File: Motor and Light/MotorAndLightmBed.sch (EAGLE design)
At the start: 97 parts, among them Q1 BSS84, Q3 BC846ASMD, Q4 220mA/50V/3.5Ω, Q5 220mA/50V/3.5Ω, Q6 220mA/50V/3.5Ω, Q7 220mA/50V/3.5Ω, U1 9DoF IMU, U2 LPC1768FBD100, X1 2510-, X2 2510-, X3 C-GRID-05-15-91, X4 C-GRID-05-15-91, X5 C-GRID-02-70553, X6 MINI-USB_4P-32005-101, Y1 32.768kHz

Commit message: Ethernet Chip added
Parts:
- added C15, C16: 100nF, rcl:C-USC0603
- added C17, C18: 100nF, resistor:C-USC0603
- added R14, R16, R17, R18: 49.9, rcl:R-US_R0603
- added U$2: DP83848JSQ/NOPB, DigiKey:DP83848JSQ/NOPB
- added X7: 22-23-2041, con-molex:22-23-2041
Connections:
- new net N$11: C18.1, U$2.AVDD33
- new net N$12: U$2.PFBOUT
- new net PFBOUT: C17.1, U$2.PFBIN1
- new net RD+: R16.1, U$2.RD+, X7-3.S
- new net RD-: R14.2, U$2.RD-, X7-4.S
- new net TD+: R18.1, U$2.TD+, X7-1.S
- new net TD-: R17.2, U$2.TD-, X7-2.S
- net +3V3: now also C15.1, C16.1, R14.1, R16.2, R17.1, R18.2
- net GND: now also C15.2, C16.2, C17.2, C18.2, U$2.AGND, U$2.AGND_2
- net SCL: now also U2.P0[20]/DTR1/SCL1
- net SDA: now also U2.P0[19]/DSR1/SDA1
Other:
- note added: "Add Ethernet"
- note added: "Analog"
- note added: "Digital into the Chip"
- moved on the sheet: J1, X1-1, X1-10, X1-2, X1-3, X1-4, X1-5, X1-6, X1-7, X1-8, X1-9, X2-1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

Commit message: First Version Completed
Several Questions remain, mbed microcontroller not included, TD, RD, +-
and D+- from ethernet Phy and main chip not connected, some pin
connection requires verification.
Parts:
- removed X6: MINI-USB_4P-32005-101, con-cypressindustries:MINI-USB_4P-32005-101
- added C19, C20, C23, C24, C25, C26: 100nF, resistor:C-USC0603
- added C21, C22: 10uF, SparkFun-Capacitors:10UF-POLAR-0603-6.3V-20%(TANT)
- added C27: 100nF, rcl:C-USC0603
- added D1, D2, D3, D4: BLUE, SparkFun-LED:LED-BLUE0603
- added J6: 6_PIN_SERIAL_CABLEPTH, SparkFun-Connectors:6_PIN_SERIAL_CABLEPTH
- added R19: 4870, rcl:R-US_R0603
- added R20: 2.2k, rcl:R-US_R0603
- added R21, R22, R23, R24: 220, resistor:R-US_R0603
- added R25, R26, R27, R28: 10k, SparkFun-Resistors:10KOHM-0603-1/10W-1%
- added R29: 100k, SparkFun-Resistors:100KOHM-0603-1/10W-1%
- added Y2: OSCILLATORSMD-5X3-50MHz, SparkFun-Clocks:OSCILLATORSMD-5X3
- added Y3: OSCILLATORSMD-5X3-12MHz, SparkFun-Clocks:OSCILLATORSMD-5X3
- U$1: value (none) -> 10uH
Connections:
- net SCON renamed TGT_SCON
- removed net N$12: U$2.PFBOUT
- removed net N$56: T1.C
- removed net N$57: T9.C
- removed net N$58: T7.C
- removed net RESET: C12.1, R15.1, S1.1
- removed net RXD: J5.7, U2.P0[25]/AD0[2]/I2SRX_SDA/TXD3
- removed net TCK: J5.4, U2.TCK/SWDCLK
- new net CLK: U$2.X1, U2.P1[15]/ENET_REF_CLK, Y2.OUT
- new net ETH_OSC_EN: U2.P1[27]/CLKOUT/!USB_OVRCR/CAP0[1], Y2.EN
- new net ETH_RST: U$2.RESET_N, U2.P1[28]/MCOA2/PCAP1[0]/MAT0[0]
- new net LED-1: R21.1, U2.P1[18]/USB_UP_LED/PWM1[1]/CAP1[0]
- new net LED-2: R22.1, U2.P1[20]/MCI0/PWM1[2]/SCK0
- new net LED-3: R23.1, U2.P1[21]/!MCABORT/PWM1[3]/SSEL0
- new net LED-4: R24.1, U2.P1[23]/MCI1/PWM1[4]/MISO0
- new net LED_LINK: U$2.LED_LINK/AN0, U2.P1[25]/MCOA1/MAT1[1]
- new net LED_SPEED: U$2.LED_SPEED/AN1, U2.P1[26]/MCOB1/PWM1[6]/CAP0[0]
- new net N$14: R19.1, U$2.RBIAS
- new net N$16: R20.2, U$2.RX_DV/MII_MODE
- new net N$17: D1.A, R21.2
- new net N$18: D2.A, R22.2
- new net N$19: D3.A, R23.2
- new net N$20: D4.A, R24.2
- new net RTCK: J5.7, R25.1, U2.RTCK
- new net TCLK: J5.4, R26.1, U2.TCK/SWDCLK
- new net TGT_P1.0: U$2.TXD_0, U2.P1[0]/ENET_TXD0
- new net TGT_P1.1: U$2.TXD_1, U2.P1[1]/ENET_TXD1
- new net TGT_P1.10: U$2.RXD_1/PHYAD2, U2.P1[10]/ENET_RXD1
- new net TGT_P1.14: U$2.RX_ER/MDIX_EN, U2.P1[14]/ENET_RX_ER
- new net TGT_P1.16: U$2.MDC, U2.P1[16]/ENET_MDC
- new net TGT_P1.17: U$2.MDIO, U2.P1[17]/ENET_MDIO
- new net TGT_P1.4: U$2.TX_EN, U2.P1[4]/ENET_TX_EN
- new net TGT_P1.8: U$2.CRS/CRS_DV/LED_CFG, U2.P1[8]/ENET_CRS
- new net TGT_P1.9: U$2.RXD_0/PHYAD1, U2.P1[9]/ENET_RXD0
- new net TGT_RXD: J6.3, U2.P0[3]/RXD0/AD0[6]
- new net TGT_TXD: J6.2, U2.P0[2]/TXD0/AD0[7]
- new net TRST: U2.!TRST
- net +3V3: now also C20.1, C22.+, C23.1, C24.1, C26.1, R20.1, R25.2, R27.2, R28.1, R29.2, U$2.IOVDD33, U$2.IOVDD33_2, Y2.VCC, Y3.EN, Y3.VCC; no longer J5.1
- net 12MHZ: now also Y3.OUT
- net 1S1: now also U2.P0[15]/TXD1/SCK0/SCK
- net 1S2: now also U2.P0[16]/RXD1/SSEL0/SSEL
- net 1S3: now also U2.P0[17]/CTS1/MISO0/MISO
- net 2S1: now also U2.P0[18]/DCD1/MOSI0/MOSI
- net 2S2: now also U2.P0[21]/RI1/RD1
- net 2S3: now also U2.P0[22]/RTS1/TD1
- net BATTIN: now also U2.P2[6]/PCAP1[0]/RI1/TRACECLK
- net GND: now also C19.2, C20.2, C21.-, C22.-, C23.2, C24.2, C25.2, C26.2, C27.2, D1.C, D2.C, D3.C, D4.C, J6.6, R19.2, R26.2, T1.C, T7.C, T9.C, U$2.DAP, U$2.DGND, U$2.IOGND, U1.AD0/SDO, Y2.GND, Y3.GND
- net LDIR: now also U2.P2[1]/PWM1[2]/RXD1
- net LDISABLE: now also U2.P2[2]/PWM1[3]/CTS1/TRACEDATA[3]
- net LEA3: now also U2.P0[4]/I2SRX_CLK/RD2/CAP2[0]
- net LEB3: now also U2.P0[5]/I2SRX_WS/TD2/CAP2[1]
- net LSPEED: now also U2.P2[0]/PWM1[1]/TXD1
- net NRESET: now also C12.1, C27.1, R15.1, R29.1, S1.1, U2.!RESET; no longer U2.!TRST
- net PFBOUT: now also C19.1, C21.+, C25.1, U$2.PFBIN2, U$2.PFBOUT
- net RDIR: now also U2.P2[4]/PWM1[5]/DSR1/TRACEDATA[1]
- net RDISABLE: now also U2.P2[5]/PWM1[6]/DTR1/TRACEDATA[0]
- net REA3: now also U2.P0[6]/I2SRX_SDA/SSEL1/MAT2[0]
- net REB3: now also U2.P0[7]/I2STX_CLK/SCK1/MAT2[1]
- net RSPEED: now also U2.P2[3]/PWM1[4]/DCD1/TRACEDATA[2]
- net TDI: now also R28.2
- net TMS: now also R27.1
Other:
- note added: "D+ and D- going in/out any stuff?"
- note added: "Questionable"
- note added: "need to verify this"
- note removed: "Add Ethernet"
- note removed: "Analog"
- note removed: "Digital into the Chip"
- moved on the sheet: C15, C16, R14, R16, R17, R18, X3-1, X3-2, X3-3, X3-4, X3-5, X4-1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

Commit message: final version v2.0
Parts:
- removed X7: 22-23-2041, con-molex:22-23-2041
- added C28, C29: 0.1uF, SparkFun-Capacitors:0.1UF-0603-25V-(+80/-20%)
- added J7: (no value), SparkFun-Connectors:USB_MICRO-B_FEMALE-SMT
- added R30, R31: 33, SparkFun-Resistors:33OHM-0603-1/10W-1%
- added R32, R33: 150, SparkFun-Resistors:150OHM-0603-1/10W-1%
- added U$3: V_REG_LD1117VXX, SparkFun-IC-Power:V_REG_LD1117VXX
- added X6: SI-50170, con-stewart:SI-50170
- R19: value 4870 -> 4.87k
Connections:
- net CLK renamed 50MHZ
- new net ETH_LED1: R32.2, X6.A
- new net ETH_LED2: R33.2, X6.A1
- new net N$15: R33.1, U2.P0[5]/I2SRX_WS/TD2/CAP2[1]
- net +3V3: now also C18.1, C28.1, C29.1, U$2.AVDD33, U$3.OUT, X6.RCT, X6.TCT
- net +5V: now also J7.VBUS, U$3.IN
- net BATTIN: now also U2.P0[26]/AD0[3]/AOUT/RXD3; no longer U2.P2[6]/PCAP1[0]/RI1/TRACECLK
- net GND: now also C28.2, C29.2, J7.GND, J7.SHIELD, U$3.GND, X6.C, X6.C1, X6.S1, X6.S2
- net GYRO_INT: now also U2.P2[10]/!EINT0/NMI
- net LEA3: now also U2.P0[8]/I2STX_WS/MISO1/MAT2[2]; no longer U2.P0[4]/I2SRX_CLK/RD2/CAP2[0]
- net LEB3: now also U2.P0[9]/I2STX_SDA/MOSI1/MAT2[3]; no longer U2.P0[5]/I2SRX_WS/TD2/CAP2[1]
- net LPC_D+: now also J7.D+, R30.1, R30.2
- net LPC_D-: now also J7.D-, R31.1, R31.2
- net N$11: now also R32.1, U2.P0[4]/I2SRX_CLK/RD2/CAP2[0]; no longer C18.1, U$2.AVDD33
- net RD+: now also X6.RD+; no longer X7-3.S
- net RD-: now also X6.RD-; no longer X7-4.S
- net TD+: now also X6.TD+; no longer X7-1.S
- net TD-: now also X6.TD-; no longer X7-2.S
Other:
- note removed: "D+ and D- going in/out any stuff?"
- note removed: "Questionable"
- moved on the sheet: C19, C21, R19

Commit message: Motor and Light Initial Submit
Primary structure completed, resistors and capacitors remained to add
and some general arrangement issues to be resolved.
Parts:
- removed OK2: MOCD208M, optocoupler:MOCD208M
- removed R12, R13, R3, R6: 1k, SparkFun-Resistors:1KOHM-0603-1/10W-1%
- removed R20: 2.2k, rcl:R-US_R0603
- added R34: 200, SparkFun-Resistors:200OHM-0603-1/10W-1%
- C15, C16: value 100nF -> 0.1uF; device rcl:C-USC0603 -> SparkFun-Capacitors:0.1UF-0603-25V-5%
- C17, C18, C19, C20, C24, C25, C26: value 100nF -> 0.1uF; device resistor:C-USC0603 -> SparkFun-Capacitors:0.1UF-0603-25V-5%
- C23: value 100nF -> 0.1uF; device resistor:C-USC0603 -> SparkFun-Capacitors:0.1UF-0603-25V-(+80/-20%)
- C27: value 100nF -> 0.1uF; device rcl:C-USC0603 -> SparkFun-Capacitors:0.1UF-0603-25V-(+80/-20%)
- R21, R22, R23: value 220 -> 200; device resistor:R-US_R0603 -> SparkFun-Resistors:200OHM-0603-1/10W-1%
- R24: value 220 -> 2.2k; device resistor:R-US_R0603 -> SparkFun-Resistors:2.2KOHM-0603-1/10W-1%
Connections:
- removed net LDISABLEI: R6.1
- removed net N$5: OK2A.A, R3.2
- removed net N$8: OK2B.A, R6.2
- removed net RDISABLEI: R3.1
- removed net VDD: C5.1, C6.1, C7.1, C8.1, C9.+, U$1.P$2, U2.NC, U2.VBAT, U2.VDD, U2.VDD_2, U2.VDD_3, U2.VDD_4, U2.VDD_5, U2.VDD_6
- net +3V3: now also C15.2, C16.2, C20.2, C23.2, C5.1, C6.1, C7.1, C8.1, C9.+, R24.2, U$1.P$2, U2.NC, U2.VBAT, U2.VDD, U2.VDD_2, U2.VDD_3, U2.VDD_4, U2.VDD_5, U2.VDD_6; no longer C15.1, C16.1, C20.1, C23.1, R20.1
- net GND: now also C15.1, C16.1, C17.1, C20.1, C23.1; no longer C15.2, C16.2, C17.2, C20.2, C23.2, OK2A.C, OK2B.C
- net LDISABLE: no longer OK2B.EMIT, R12.2
- net LED-1: now also R34.1; no longer R21.1
- net LED-2: now also R21.1; no longer R22.1
- net LED-3: now also R22.1; no longer R23.1
- net LED-4: now also R23.1; no longer R24.1
- net LGND: no longer R12.1
- net LVCC: no longer OK2B.COL
- net N$16: now also R24.1; no longer R20.2
- net N$17: now also R34.2; no longer R21.2
- net N$18: now also R21.2; no longer R22.2
- net N$19: now also R22.2; no longer R23.2
- net N$20: now also R23.2; no longer R24.2
- net PFBOUT: now also C17.2; no longer C17.1
- net RDISABLE: no longer OK2A.EMIT, R13.2
- net RGND: no longer R13.1
- net RVCC: no longer OK2A.COL
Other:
- moved on the sheet: C15, C16, C17, C20, C23, R21, R22, R23, R24

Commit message: Updated Board Design
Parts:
- removed U$3: V_REG_LD1117VXX, SparkFun-IC-Power:V_REG_LD1117VXX
- added CR1: LD1117S33TR, LD1117:LD1117S33TR
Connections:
- new net USB_D+: C10.1, R1.2, R30.2, U2.P0[29]/USB_D+
- new net USB_D-: C11.1, R31.2, U2.P0[30]/USB_D?
- net +3V3: now also CR1.OUTPUT; no longer U$3.OUT
- net +5V: now also CR1.INPUT; no longer U$3.IN
- net GND: now also CR1.GROUND; no longer U$3.GND
- net LEA3: now also U2.P2[11]/!EINT1/I2STX_CLK; no longer U2.P0[8]/I2STX_WS/MISO1/MAT2[2]
- net LPC_D+: no longer C10.1, R1.2, R30.2, U2.P0[29]/USB_D+
- net LPC_D-: no longer C11.1, R31.2, U2.P0[30]/USB_D?
- net REA3: now also U2.P2[12]/!EINT2/I2STX_WS; no longer U2.P0[6]/I2SRX_SDA/SSEL1/MAT2[0]
- net REB3: now also U2.P0[8]/I2STX_WS/MISO1/MAT2[2]; no longer U2.P0[7]/I2STX_CLK/SCK1/MAT2[1]

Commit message: update
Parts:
- added R3, R6: 2700, SparkFun-Resistors:3.9KOHM-0603-1/10W-1%
- added T10: (no value), transistor:-NPN-TO220V
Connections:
- new net N$24: J4.1, R6.1, T10.C
- net +12V: now also R6.2
- net ESTOP: now also R3.2, U2.P0[0]/RD1/TXD3/SDA1
- net GND: now also R3.1, T10.E
- net SLIGHT: now also T10.B, U2.P0[1]/TD1/RXD3/SCL1; no longer J4.1
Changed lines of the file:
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@@
 <part name="C23" library="SparkFun-Capacitors" deviceset="0.1UF" device="-0603-25V-(+80/-20%)" value="0.1uF"/>
 <part name="CR1" library="LD1117" deviceset="LD1117S33TR" device=""/>
+<part name="R3" library="SparkFun-Resistors" deviceset="3.9KOHM" device="-0603-1/10W-1%" value="2700"/>
+<part name="GND6" library="supply1" deviceset="GND" device=""/>
+<part name="T10" library="transistor" deviceset="*-NPN-" device="TO220V"/>
+<part name="GND9" library="supply1" deviceset="GND" device=""/>
+<part name="R6" library="SparkFun-Resistors" deviceset="3.9KOHM" device="-0603-1/10W-1%" value="2700"/>
+<part name="P+3" library="supply1" deviceset="+12V" device=""/>
 </parts>
 <sheets>
@@
 <instance part="C23" gate="G$1" x="276.86" y="101.6"/>
 <instance part="CR1" gate="A" x="114.3" y="177.8"/>
+<instance part="R3" gate="G$1" x="505.46" y="355.6" rot="R90"/>
+<instance part="GND6" gate="1" x="505.46" y="345.44"/>
+<instance part="T10" gate="G$1" x="444.5" y="358.14"/>
+<instance part="GND9" gate="1" x="447.04" y="342.9"/>
+<instance part="R6" gate="G$1" x="447.04" y="373.38" rot="R90"/>
+<instance part="P+3" gate="1" x="447.04" y="386.08"/>
 </instances>
 <busses>
@@
 <wire x1="177.8" y1="175.26" x2="180.34" y2="175.26" width="0.1524" layer="91"/>
 </segment>
+<segment>
+<pinref part="R3" gate="G$1" pin="1"/>
+<pinref part="GND6" gate="1" pin="GND"/>
+<wire x1="505.46" y1="350.52" x2="505.46" y2="347.98" width="0.1524" layer="91"/>
+</segment>
+<segment>
+<pinref part="T10" gate="G$1" pin="E"/>
+<pinref part="GND9" gate="1" pin="GND"/>
+<wire x1="447.04" y1="353.06" x2="447.04" y2="345.44" width="0.1524" layer="91"/>
+</segment>
 </net>
 <net name="N$1" class="0">
@@
 <wire x1="462.28" y1="332.74" x2="469.9" y2="332.74" width="0.1524" layer="91"/>
 </segment>
+<segment>
+<pinref part="P+3" gate="1" pin="+12V"/>
+<pinref part="R6" gate="G$1" pin="2"/>
+<wire x1="447.04" y1="383.54" x2="447.04" y2="378.46" width="0.1524" layer="91"/>
+</segment>
 </net>
 <net name="RED" class="0">
@@
 <segment>
 <pinref part="X5" gate="-1" pin="S"/>
-<wire x1="510.54" y1="365.76" x2="500.38" y2="365.76" width="0.1524" layer="91"/>
+<wire x1="510.54" y1="365.76" x2="505.46" y2="365.76" width="0.1524" layer="91"/>
 <label x="500.38" y="365.76" size="1.778" layer="95"/>
+<pinref part="R3" gate="G$1" pin="2"/>
+<wire x1="505.46" y1="365.76" x2="500.38" y2="365.76" width="0.1524" layer="91"/>
+<wire x1="505.46" y1="365.76" x2="505.46" y2="360.68" width="0.1524" layer="91"/>
+</segment>
+<segment>
+<pinref part="U2" gate="A" pin="P0[0]/RD1/TXD3/SDA1"/>
+<wire x1="121.92" y1="231.14" x2="106.68" y2="231.14" width="0.1524" layer="91"/>
+<label x="106.68" y="231.14" size="1.778" layer="95"/>
 </segment>
 </net>
 <net name="SLIGHT" class="0">
 <segment>
-<pinref part="J4" gate="G$1" pin="1"/>
-<wire x1="469.9" y1="365.76" x2="462.28" y2="365.76" width="0.1524" layer="91"/>
-<label x="459.74" y="365.76" size="1.778" layer="95"/>
+<pinref part="U2" gate="A" pin="P0[1]/TD1/RXD3/SCL1"/>
+<wire x1="121.92" y1="228.6" x2="106.68" y2="228.6" width="0.1524" layer="91"/>
+<label x="106.68" y="228.6" size="1.778" layer="95"/>
+</segment>
+<segment>
+<wire x1="426.72" y1="358.14" x2="441.96" y2="358.14" width="0.1524" layer="91"/>
+<pinref part="T10" gate="G$1" pin="B"/>
+<label x="429.26" y="358.14" size="1.778" layer="95"/>
 </segment>
 </net>
@@
 </segment>
 </net>
+<net name="N$24" class="0">
+<segment>
+<pinref part="R6" gate="G$1" pin="1"/>
+<pinref part="T10" gate="G$1" pin="C"/>
+<wire x1="447.04" y1="368.3" x2="447.04" y2="365.76" width="0.1524" layer="91"/>
+<pinref part="J4" gate="G$1" pin="1"/>
+<wire x1="447.04" y1="365.76" x2="447.04" y2="363.22" width="0.1524" layer="91"/>
+<wire x1="469.9" y1="365.76" x2="447.04" y2="365.76" width="0.1524" layer="91"/>
+</segment>
+</net>

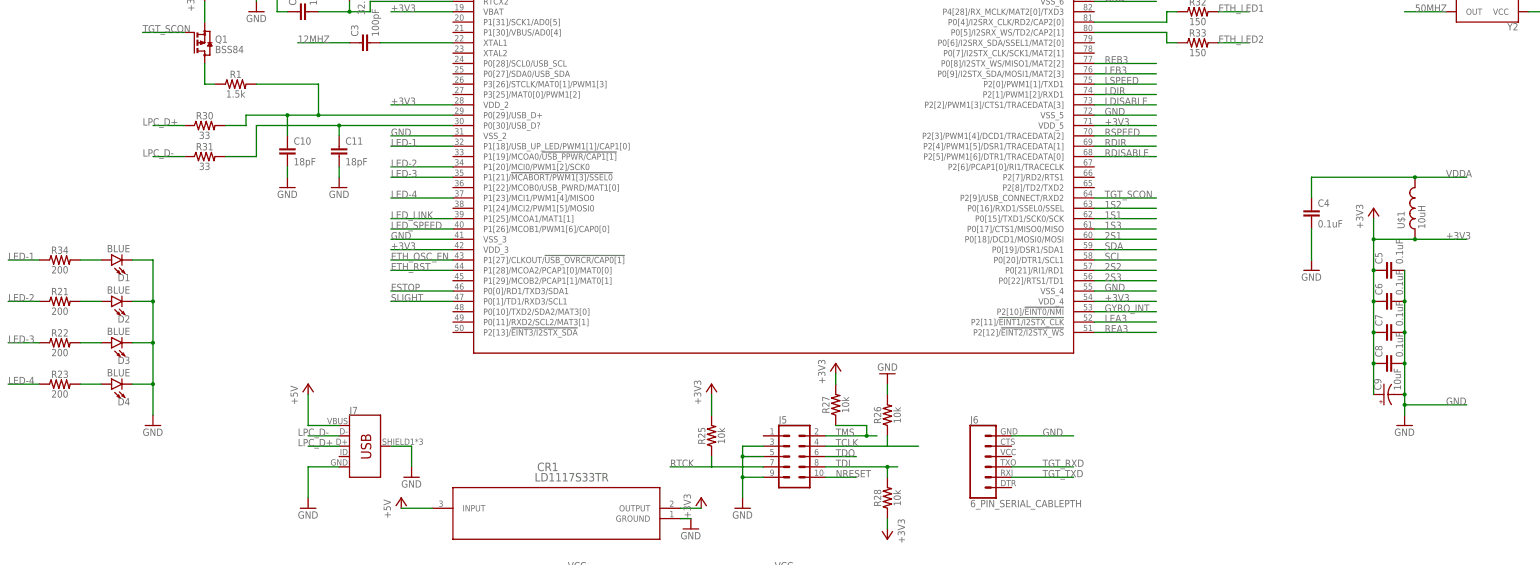
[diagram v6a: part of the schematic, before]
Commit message: Finalized
Final Submission before design review. IMU problem remain unresolved.
Micro-usb-b addressed.
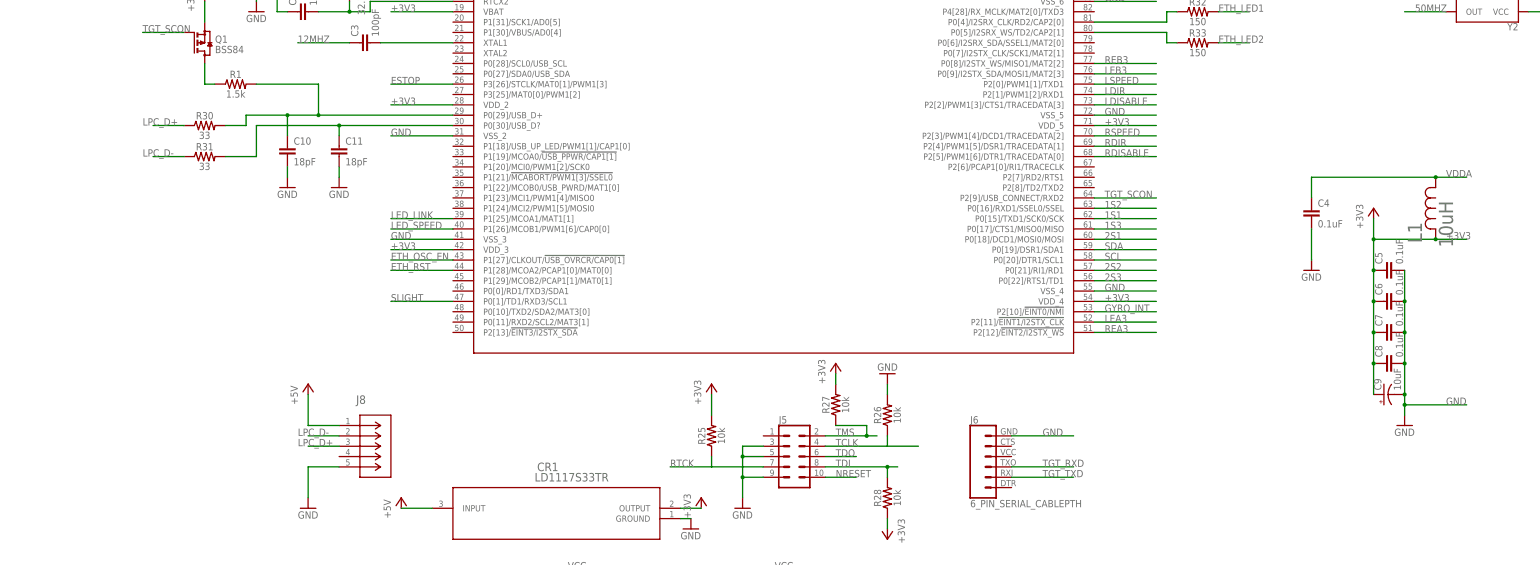
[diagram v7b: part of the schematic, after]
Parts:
- removed D1, D2, D3, D4: BLUE, SparkFun-LED:LED-BLUE0603
- removed J7: (no value), SparkFun-Connectors:USB_MICRO-B_FEMALE-SMT
- removed R21, R22, R23, R34: 200, SparkFun-Resistors:200OHM-0603-1/10W-1%
- removed U$1: 10uH, inductor-coilcraft:MSS1260
- added J8: 1981568-1, DigiKey:1981568-1
- added L1: 10uH, DigiKey:MLZ1608N100LT000
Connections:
- removed net LED-1: R34.1, U2.P1[18]/USB_UP_LED/PWM1[1]/CAP1[0]
- removed net LED-2: R21.1, U2.P1[20]/MCI0/PWM1[2]/SCK0
- removed net LED-3: R22.1, U2.P1[21]/!MCABORT/PWM1[3]/SSEL0
- removed net LED-4: R23.1, U2.P1[23]/MCI1/PWM1[4]/MISO0
- removed net N$17: D1.A, R34.2
- removed net N$18: D2.A, R21.2
- removed net N$19: D3.A, R22.2
- removed net N$20: D4.A, R23.2
- net +3V3: now also L1.2; no longer U$1.P$2
- net +5V: now also J8.1; no longer J7.VBUS
- net ESTOP: now also U2.P3[26]/STCLK/MAT0[1]/PWM1[3]; no longer U2.P0[0]/RD1/TXD3/SDA1
- net GND: now also J8.5; no longer D1.C, D2.C, D3.C, D4.C, J7.GND, J7.SHIELD
- net LPC_D+: now also J8.3; no longer J7.D+
- net LPC_D-: now also J8.2; no longer J7.D-
- net VDDA: now also L1.1; no longer U$1.P$1
